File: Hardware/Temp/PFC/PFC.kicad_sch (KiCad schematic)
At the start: 9 parts, among them J1 HB9500M-9.5-3P, U1 UCC28180D

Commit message: change schematic
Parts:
- removed C2: 100nF, 275VAC, charge_battery_footprint_lib:CAP_B32671P-10--5x11x13_TDK, symbol charge_battery_sym_lib:Film Cap
- removed CR1: MSC010SDA120K, charge_battery_footprint_lib:TO-220-2_MCH, symbol charge_battery_sym_lib:MSC010SDA120K
- added C10, C6: 100nF, 275VAC, charge_battery_footprint_lib:CAP_B32671P-10--5x11x13_TDK, symbol charge_battery_sym_lib:Film Cap
- added C11: 1uF 50V, charge_battery_footprint_lib:Ceramic_Cap_Hole_1uF_50V, symbol charge_battery_sym_lib:Ceramic_Cap_Hole_1uF_50V_
- added C12, C3: 1nF 50V, charge_battery_footprint_lib:Ceramic_Cap_Hole_1nF_50V, symbol charge_battery_sym_lib:Ceramic_Cap_Hole_1nF_50V
- added C13: 330uF_450V, charge_battery_footprint_lib:Big_Cap_330uF_450V, symbol charge_battery_sym_lib:Cap_Polarized_330uF_450V
- added C2: 47uF_16VV, charge_battery_footprint_lib:Cap_Polarized_SMD_47uF_16V, symbol charge_battery_sym_lib:Cap_Polarized_SMD_47uF_16V
- added C4, C5: 1nF 2000V, charge_battery_footprint_lib:Ceramic_Cap_Hole_1nF_2000V, symbol charge_battery_sym_lib:Ceramic_Cap_Hole_680pF_1000V
- added C7: 680pF 1000V, charge_battery_footprint_lib:Ceramic_Cap_Hole_680pF_1000V, symbol charge_battery_sym_lib:Ceramic_Cap_Hole_1nF_2000V
- added C8: 10uF_50V, Capacitor_SMD:C_0805_2012Metric, symbol charge_battery_sym_lib:Ceramic_Cap_Hole_10uF_50V
- added C9: 10uF 16V, charge_battery_footprint_lib:Ceramic_Cap_10uF_16V, symbol charge_battery_sym_lib:Ceramic_Cap_SMD_10uF_16V
- added D2: Diode_Shottky_SR5100, charge_battery_footprint_lib:Diode_Schottky_SR5100, symbol charge_battery_sym_lib:Diode_Shottky_SR5100
- added D3: 60A, 600V, charge_battery_footprint_lib:Diode_FRED_TO247, symbol charge_battery_sym_lib:Diode_DSEI60-06A_FRED_TO247
- added D4: MSC010SDA, charge_battery_footprint_lib:DBoost, symbol charge_battery_sym_lib:Diode_Shottky_DBoost
- added J2, J3: Terminal, charge_battery_footprint_lib:Terminal, symbol charge_battery_sym_lib:Terminal HB9500-2
- added L2: 680uH, Inductor_SMD:L_12x12mm_H8mm, symbol Device:L
- added M1: 600V 9.5A, charge_battery_footprint_lib:MOSFET_FQPF10N60C, symbol charge_battery_sym_lib:MOSFET_FQPF10N60C
- added R1: 18K_1/4W_1%, charge_battery_footprint_lib:Res_220R_1_4W_1%, symbol charge_battery_sym_lib:Res_hole_18K_1/4W_1%
- added R2: 18K_1/4W_5%, charge_battery_footprint_lib:Res_220R_1_4W_1%, symbol charge_battery_sym_lib:Res_hole_18K_1/4W_1%
- added R3: 220R_1/4W_1%, charge_battery_footprint_lib:Res_220R_1_4W_1%, symbol charge_battery_sym_lib:Res_hole_220R_1/4W_1%
- added R4: R_Shunt_10mR, charge_battery_footprint_lib:R_Shunt, symbol charge_battery_sym_lib:R_Shunt_10mR
- added R5: 3,3K_1/4W_1%, charge_battery_footprint_lib:Res_3.3R_1_4W_1, symbol charge_battery_sym_lib:Res_hole_3,3K_1/4W_1%
- added R6: 10K_1/4W_1%, charge_battery_footprint_lib:Res_10K_1_4W_1%, symbol charge_battery_sym_lib:Res_hole_10K_1/4W_1%
- added R7: 1M_1W_1%, charge_battery_footprint_lib:Res_1M_1W_1%, symbol charge_battery_sym_lib:Res_hole_1M_1W_1%
- added R8: 13K_1/4W_1%, charge_battery_footprint_lib:Res_13K_1_4W_1, symbol charge_battery_sym_lib:Res_hole_13K_1/4W_1%
- added TH1: 5R, charge_battery_footprint_lib:Thermistor_NTC, symbol charge_battery_sym_lib:Thermistor_NTC
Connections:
- net Earth: now also C4.1, C5.1
- net at L1.2: now also D1.2, C4.2, C6.1
- net at L1.3: now also C5.2, C6.2, TH1.1
- net GND: now reaches U1.1 (GND)
- net GND: now also C11.1, C12.1, C13.2, C2.2, C3.1, C7.1, C8.1, C9.1, J2.1, J3.2, M1.3 (S), R1.1, R4.1, R6.1, R8.1
- net at U1.2 (ICOMP): now also C3.2
- net at U1.3 (ISENSE): now also C7.2, R3.1
- net at U1.4 (FREQ): now also R1.2
- net at U1.5 (VCOMP): now also C9.2, R2.2
- net at U1.6 (VSENSE): now also C12.2, R7.1, R8.2
- net at U1.7 (VCC): now also C11.2, C2.1, J2.2
- net at U1.8 (GATE): now also D2.2 (A), R5.1
- net at D1.1: now also C10.2, D3.1, L2.1
- net at D1.3: now also C10.1, R3.2, R4.2
- net at D1.4: now also TH1.2
- new net: D2.1 (K), M1.1 (G), R5.2, R6.2
- new net: C13.1, D3.2, D4.2 (A), J3.1, R7.2
- new net: D4.1 (K), L2.2, M1.2 (D)
- new net: C8.2, R2.1

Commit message: update: schematic PFC
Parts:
- removed J2, J3: Terminal, charge_battery_footprint_lib:Terminal, symbol charge_battery_sym_lib:Terminal HB9500-2
- removed R1: 18K_1/4W_1%, charge_battery_footprint_lib:Res_220R_1_4W_1%, symbol charge_battery_sym_lib:Res_hole_18K_1/4W_1%
- removed R2: 18K_1/4W_5%, charge_battery_footprint_lib:Res_220R_1_4W_1%, symbol charge_battery_sym_lib:Res_hole_18K_1/4W_1%
- removed R3: 220R_1/4W_1%, charge_battery_footprint_lib:Res_220R_1_4W_1%, symbol charge_battery_sym_lib:Res_hole_220R_1/4W_1%
- removed R4: R_Shunt_10mR, charge_battery_footprint_lib:R_Shunt, symbol charge_battery_sym_lib:R_Shunt_10mR
- removed R5: 3,3K_1/4W_1%, charge_battery_footprint_lib:Res_3.3R_1_4W_1, symbol charge_battery_sym_lib:Res_hole_3,3K_1/4W_1%
- removed R6: 10K_1/4W_1%, charge_battery_footprint_lib:Res_10K_1_4W_1%, symbol charge_battery_sym_lib:Res_hole_10K_1/4W_1%
- removed R7: 1M_1W_1%, charge_battery_footprint_lib:Res_1M_1W_1%, symbol charge_battery_sym_lib:Res_hole_1M_1W_1%
- removed R8: 13K_1/4W_1%, charge_battery_footprint_lib:Res_13K_1_4W_1, symbol charge_battery_sym_lib:Res_hole_13K_1/4W_1%
- added R1: 13K_1/4W_1%, charge_battery_footprint_lib:Res_13K_1_4W_1, symbol charge_battery_sym_lib:Res_hole_13K_1/4W_1%
- added R10: 18K_1/4W_5%, charge_battery_footprint_lib:Res_18K_1_4W_1, symbol charge_battery_sym_lib:Res_hole_18K_1/4W_5%
- added R3: R_Shunt_10mR, charge_battery_footprint_lib:R_Shunt, symbol charge_battery_sym_lib:R_Shunt_10mR
- added R4: 3,3K_1/4W_1%, charge_battery_footprint_lib:Res_3.3R_1_4W_1, symbol charge_battery_sym_lib:Res_hole_3,3K_1/4W_1%
- added R5: 10K_1/4W_1%, charge_battery_footprint_lib:Res_10K_1_4W_1%, symbol charge_battery_sym_lib:Res_hole_10K_1/4W_1%
- added R6: Res_hole_1M_1W_1%, charge_battery_footprint_lib:Res_1M_1W_1%, symbol charge_battery_sym_lib:Res_hole_1M_1W_1%
- added R7: 18K_1/4W_1%, charge_battery_footprint_lib:Res_18K_1_4W_1, symbol charge_battery_sym_lib:Res_hole_18K_1/4W_1%
- added R9: 220R_1/4W_1%, charge_battery_footprint_lib:Res_220R_1_4W_1%, symbol charge_battery_sym_lib:Res_hole_220R_1/4W_1%
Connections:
- net GND: now also R1.1, R3.1, R5.1, R7.1
- net at U1.4 (FREQ): now also R7.2
- net at C10.1, D1.3: now also R3.2, R9.2
- net at D2.1 (K), M1.1 (G): now also R4.2, R5.2
- net at C13.1, D3.2, D4.2 (A): now also R6.2
- net at C7.2, U1.3 (ISENSE): now also R9.1
- net at D2.2 (A), U1.8 (GATE): now also R4.1
- net at C8.2: now also R10.1
- net at C9.2, U1.5 (VCOMP): now also R10.2
- net at C12.2, U1.6 (VSENSE): now also R1.2, R6.1

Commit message: completed PFC
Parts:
- added J2: Terminal, charge_battery_footprint_lib:Terminal, symbol charge_battery_sym_lib:Terminal HB9500-2
- R6: value Res_hole_1M_1W_1% -> 1M_1W_1%
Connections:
- net GND: now also J2.1
- net V_OUT_PFC: now reaches C13.1, D3.2, D4.2 (A), R6.2
- net at C11.2, C2.1, U1.7 (VCC): now also J2.2
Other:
- moved on the sheet: C1, C10, C11, C12, C13, C2, C3, C4, C5, C6, C7, C8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

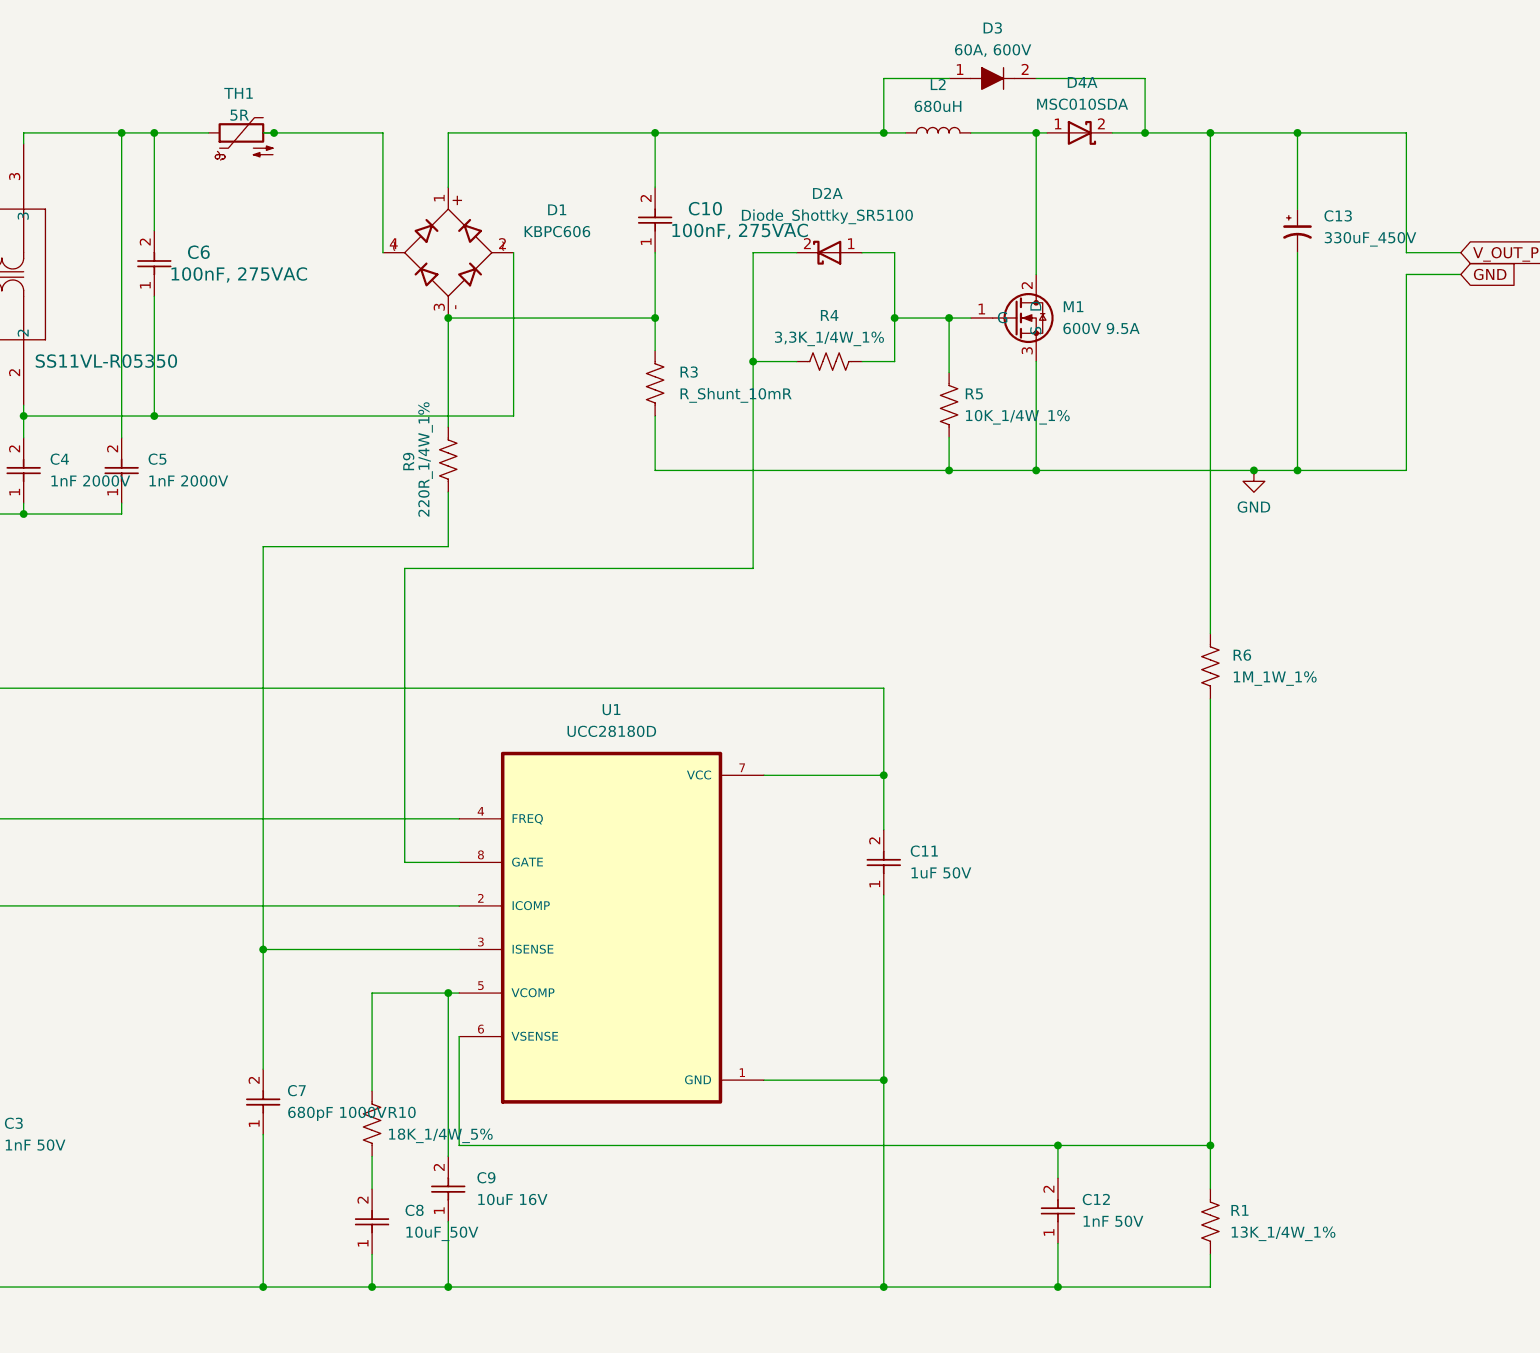
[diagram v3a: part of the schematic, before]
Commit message: update: library and fix the schematic from require of Viet but some point havenot been clarified including C8, C9, C11, R1, R10
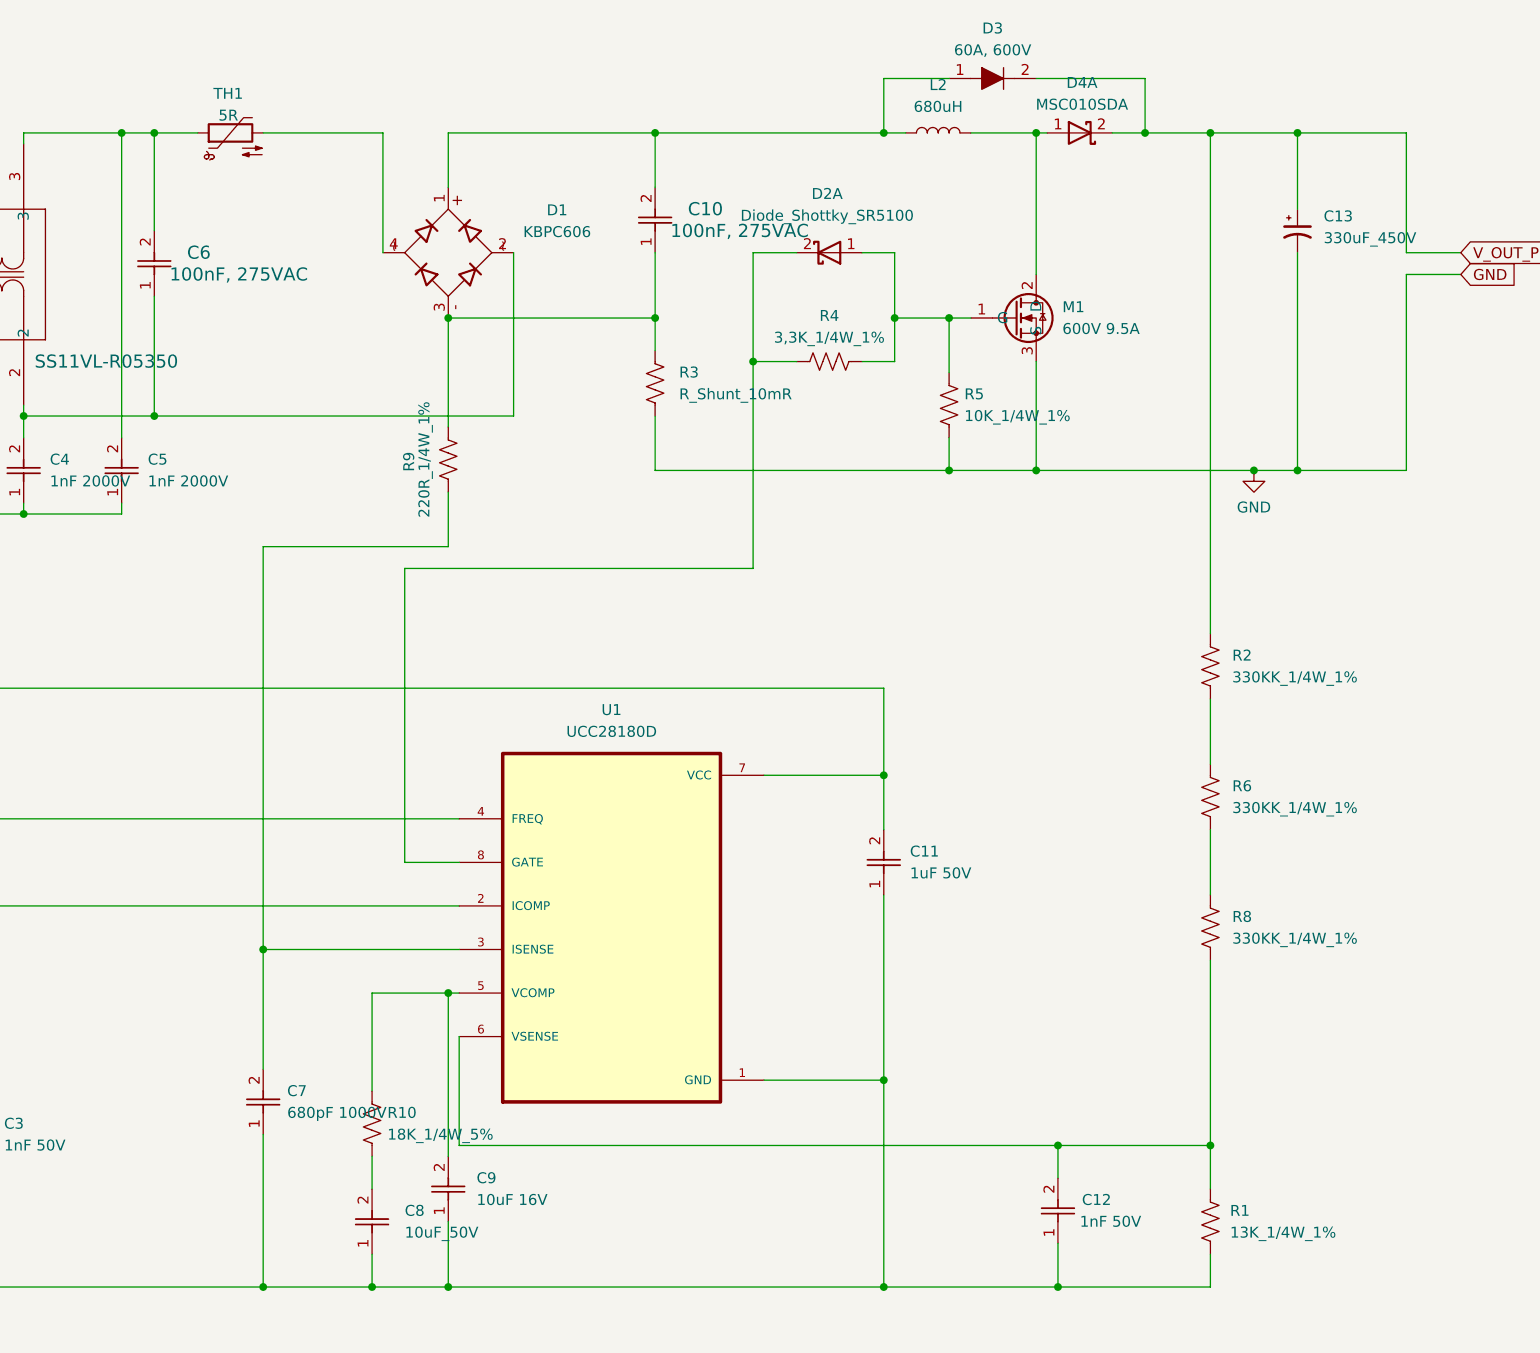
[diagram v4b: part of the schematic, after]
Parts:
- removed R6: 1M_1W_1%, charge_battery_footprint_lib:Res_1M_1W_1%, symbol charge_battery_sym_lib:Res_hole_1M_1W_1%
- added R2, R6, R8: 330KK_1/4W_1%, charge_battery_footprint_lib:Res_18K_1_4W_1, symbol charge_battery_sym_lib:Res_hole_18K_1/4W_1%
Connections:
- net V_OUT_PFC: now also R2.2
- net at C12.2, R1.2, U1.6 (VSENSE): now also R8.1
- new net: R2.1, R6.2
- new net: R6.1, R8.2
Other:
- moved on the sheet: TH1

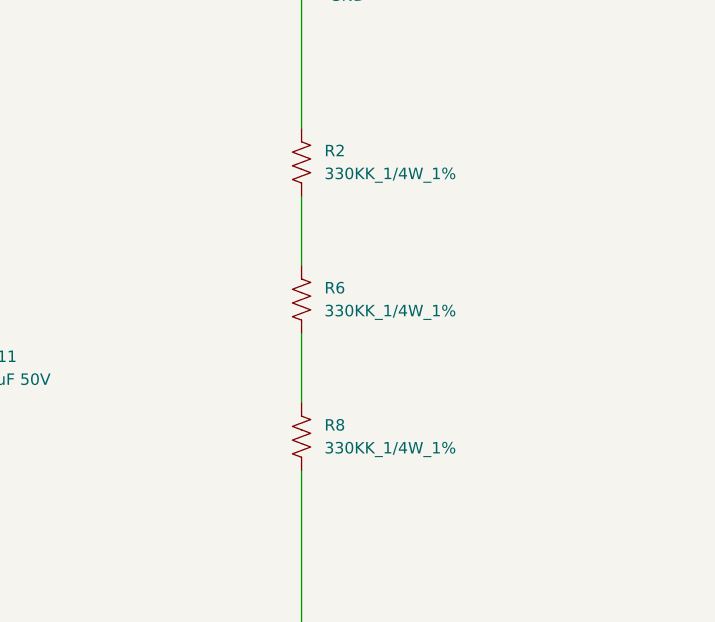
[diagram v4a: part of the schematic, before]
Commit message: re-update: library and fix the schematic from require of Viet but some point havenot been clarified including C8, C9, C11, R1, R10
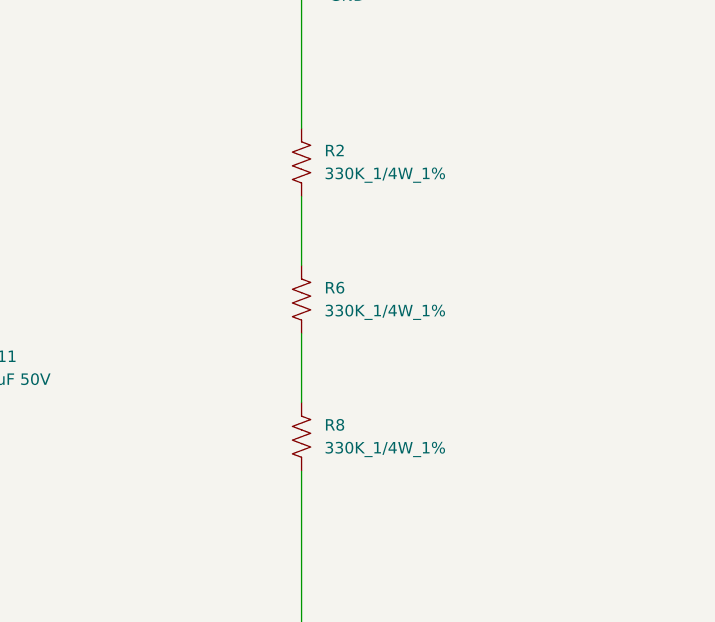
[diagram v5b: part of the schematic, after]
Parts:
- R2, R6, R8: value 330KK_1/4W_1% -> 330K_1/4W_1%
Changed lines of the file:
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@@
 			)
 		)
-		(property "Value" "330KK_1/4W_1%"
+		(property "Value" "330K_1/4W_1%"
 			(at 240.03 90.1699 90)
 			(effects
@@
 			)
 		)
-		(property "Value" "330KK_1/4W_1%"
+		(property "Value" "330K_1/4W_1%"
 			(at 240.03 120.6499 90)
 			(effects
@@
 			)
 		)
-		(property "Value" "330KK_1/4W_1%"
+		(property "Value" "330K_1/4W_1%"
 			(at 240.03 105.4099 90)
 			(effects
